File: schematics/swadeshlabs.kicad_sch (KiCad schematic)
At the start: 9 parts, among them J1 Screw_Terminal_01x02, M1 Motor_AC, U1 ACC_ADXL335, U2 ACOUS_MAX4466, U4 REG_AC_DIMMER, U5 TEMP_DS1820, U6 ESP32-S3-WROOM-1-N16R8

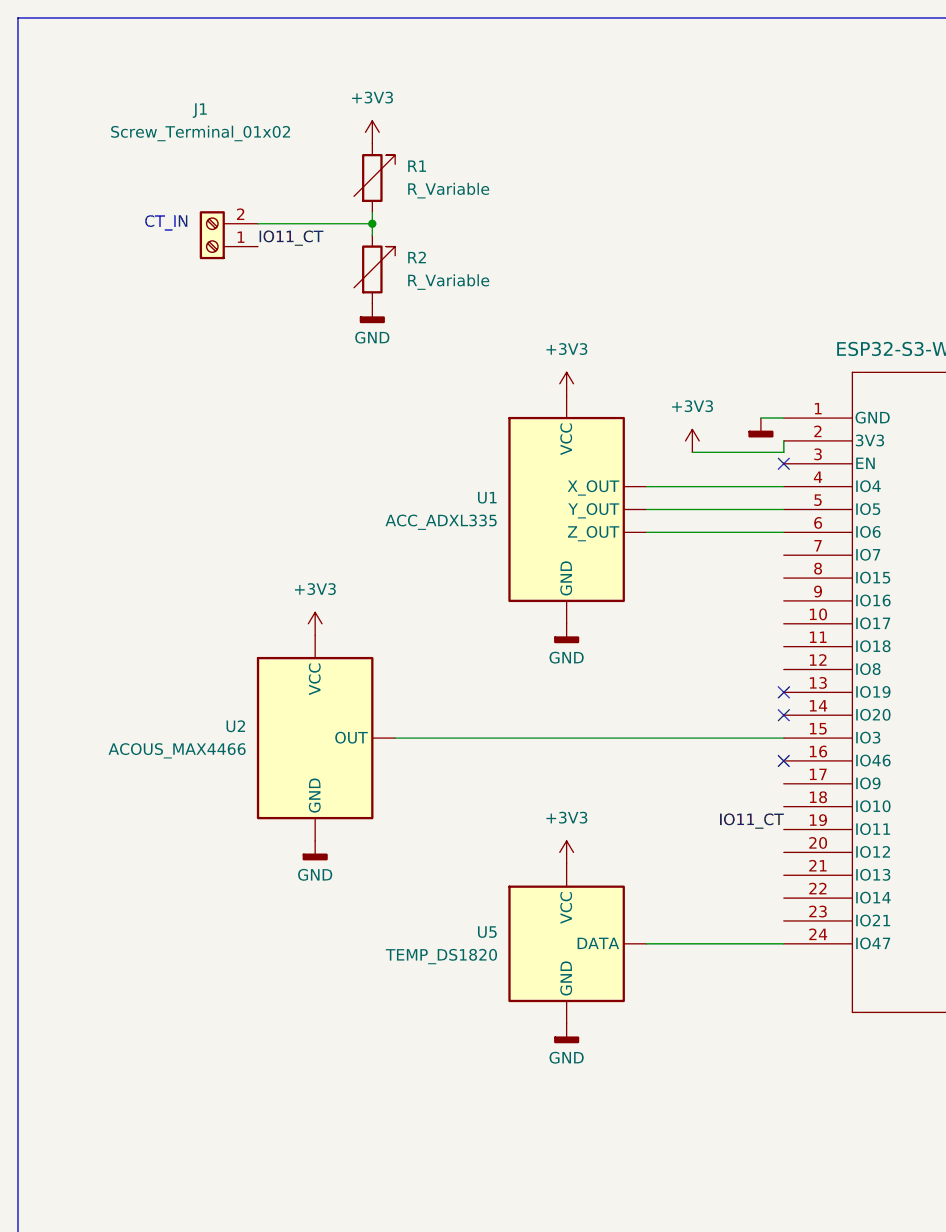
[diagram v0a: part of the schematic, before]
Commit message: 4 sensor code added
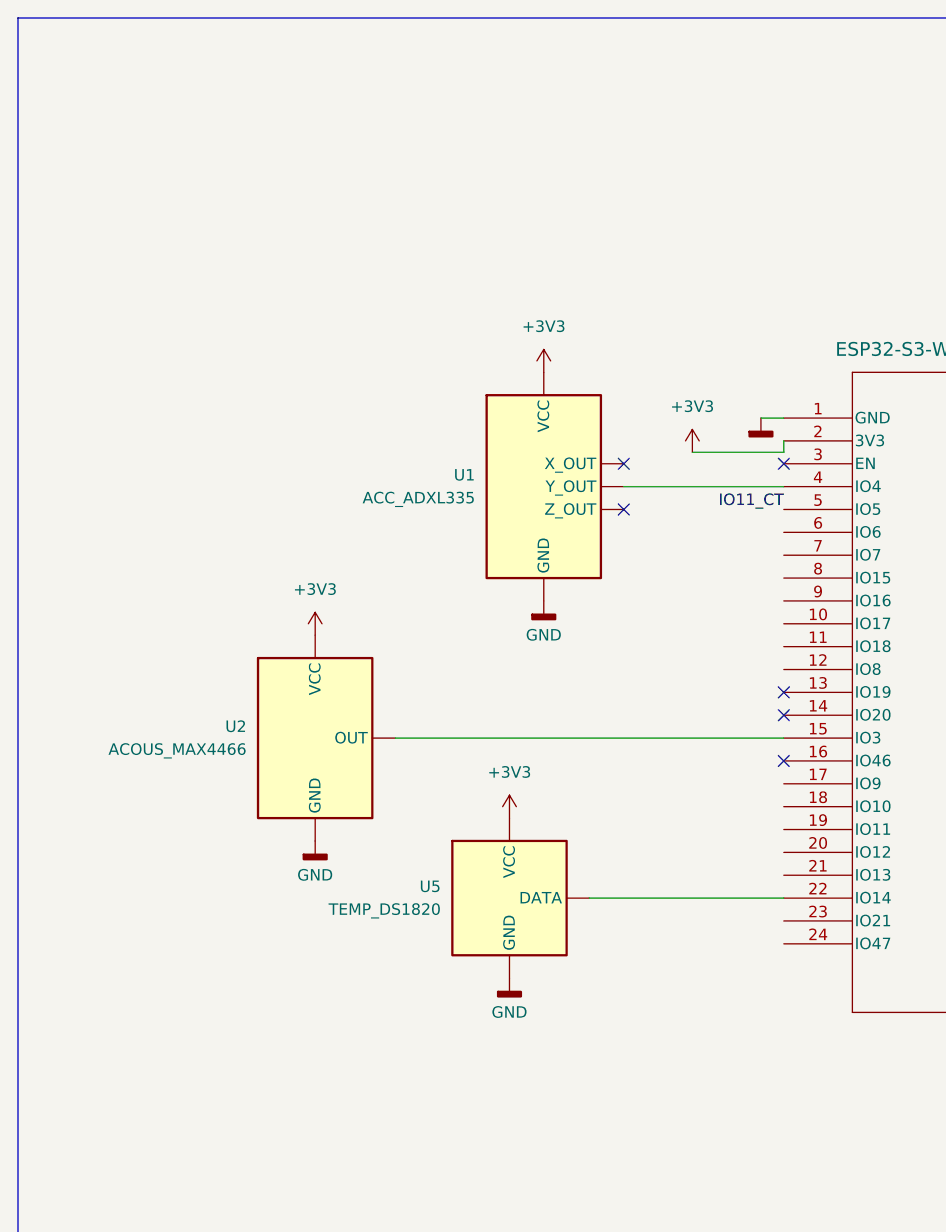
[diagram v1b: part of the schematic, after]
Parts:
- removed J1: Screw_Terminal_01x02, symbol Connector:Screw_Terminal_01x02
- removed R1, R2: R_Variable, symbol Device:R_Variable
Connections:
- net IO11_CT: now also U6.5 (IO5); no longer U6.19 (IO11)
- net at U6.24 (IO47): no longer U5. (DATA)
- net at U6.22 (IO14): now also U5. (DATA)
- net at U6.6 (IO6): no longer U1. (Z_OUT)
- no-connect marks 11 -> 13
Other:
- note removed: "CT_IN"
- moved on the sheet: U1, U5
